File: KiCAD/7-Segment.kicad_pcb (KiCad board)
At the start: 2 copper layers, 94.5 x 100 mm, 26 parts, among them J1 3Pin_Fem, J2 3Pin_Male, J3 3Pin_Fem, J4 3Pin_Male, J5 3Pin_Fem, J6 3Pin_Male, J7 3Pin_Fem, J8 3Pin_Male

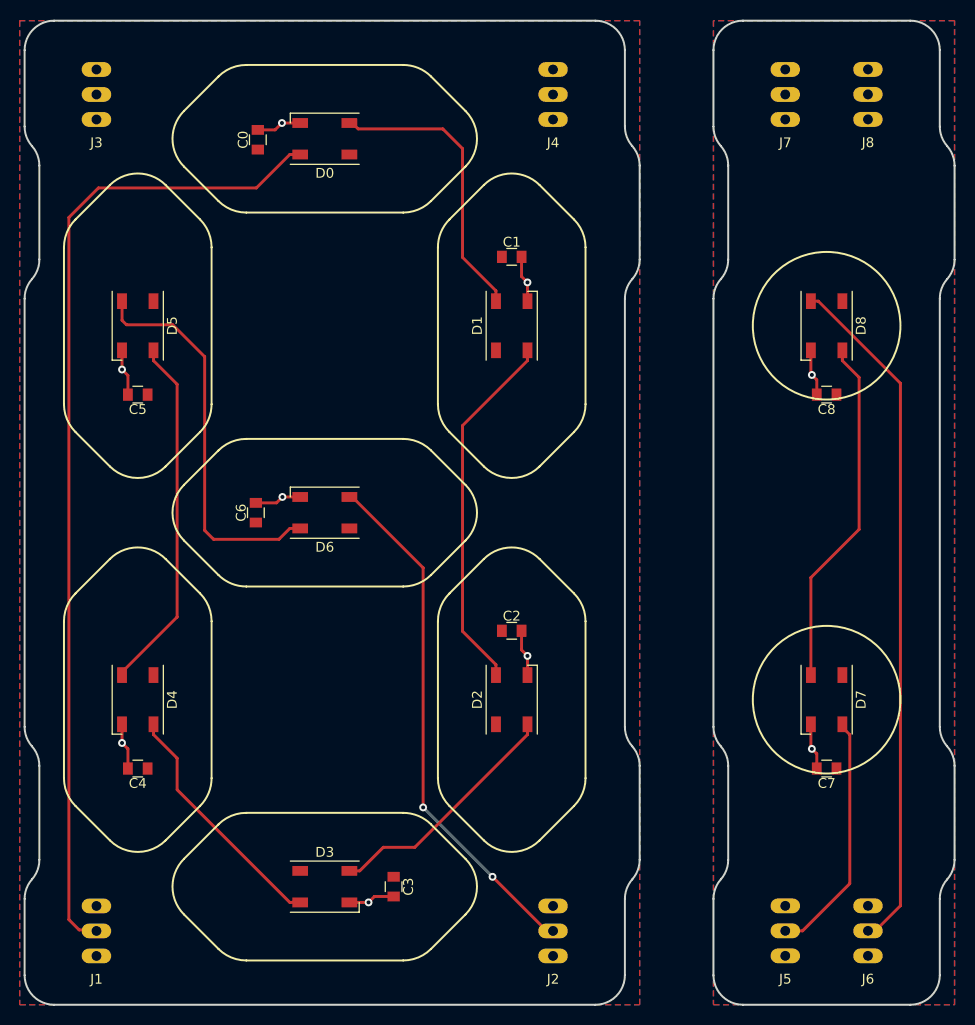
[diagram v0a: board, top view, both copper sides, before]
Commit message: 2-LED per segment
Changed from 1 to 2 LEDs per segment. Removed caps per LED and included 2 placeholder caps for the module.
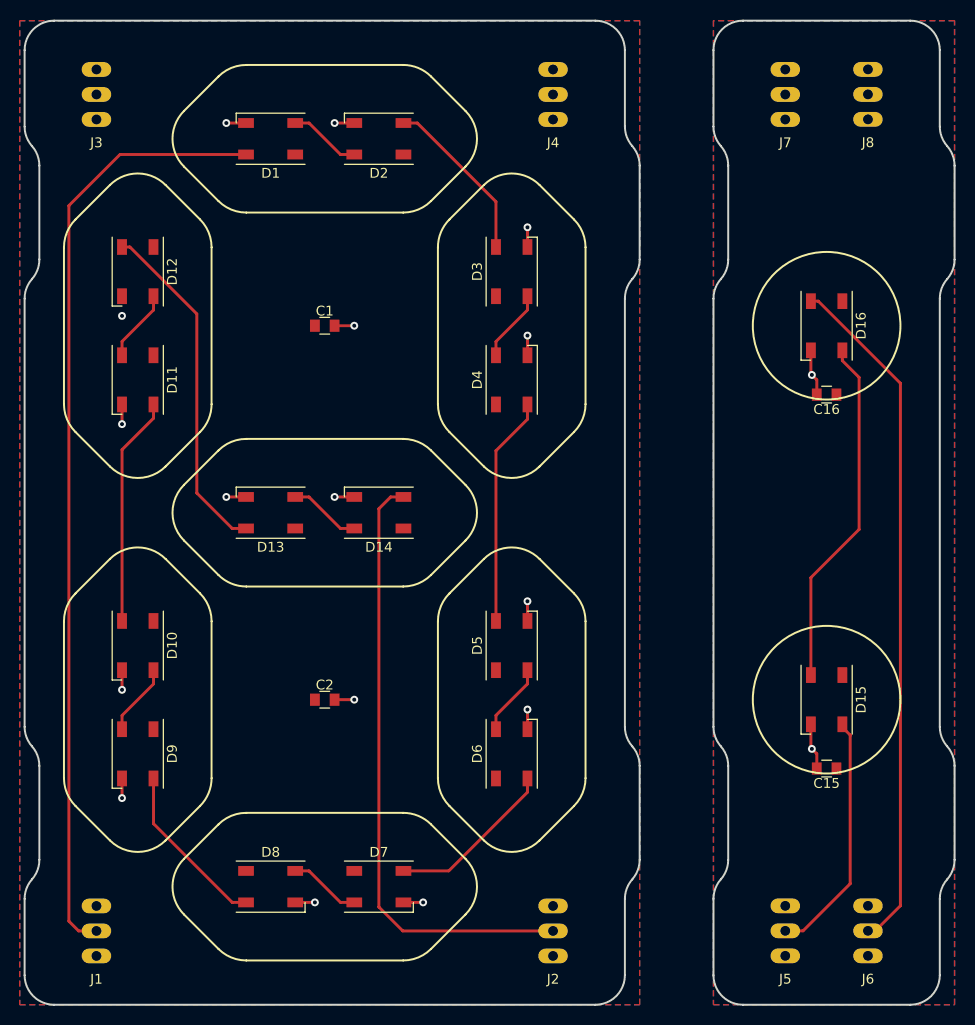
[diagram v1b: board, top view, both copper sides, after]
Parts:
- removed C0, C3, C4, C5, C6, C7, C8: C_Small, Capacitors_SMD:C_0805
- removed D0: WS2812B, LEDs:LED_WS2812B-PLCC4
- added C15: C_Small, Capacitors_SMD:C_0805, F.Cu at (133.0, 125.0)
- added C16: C_Small, Capacitors_SMD:C_0805, F.Cu at (133.0, 87.0)
- added D10: WS2812B, LEDs:LED_WS2812B-PLCC4, F.Cu at (63.0, 112.5)
- added D11: WS2812B, LEDs:LED_WS2812B-PLCC4, F.Cu at (63.0, 85.5)
- added D12: WS2812B, LEDs:LED_WS2812B-PLCC4, F.Cu at (63.0, 74.5)
- added D13: WS2812B, LEDs:LED_WS2812B-PLCC4, F.Cu at (76.5, 99.0)
- added D14: WS2812B, LEDs:LED_WS2812B-PLCC4, F.Cu at (87.5, 99.0)
- added D15: WS2812B, LEDs:LED_WS2812B-PLCC4, F.Cu at (133.0, 118.0)
- added D16: WS2812B, LEDs:LED_WS2812B-PLCC4, F.Cu at (133.0, 80.0)
- added D9: WS2812B, LEDs:LED_WS2812B-PLCC4, F.Cu at (63.0, 123.5)
- moved D8 80.3 mm to (76.5, 137.0), turned to 0 degrees
- moved D3 65.3 mm to (101.0, 74.5), turned to 90 degrees
- moved D2 58.6 mm to (87.5, 61.0), turned to 180 degrees
- moved D4 50.0 mm to (101.0, 85.5), turned to 90 degrees
- moved D5 50.0 mm to (101.0, 112.5), turned to 90 degrees
- moved D7 49.3 mm to (87.5, 137.0), turned to 0 degrees
- moved D1 31.0 mm to (76.5, 61.0), turned to 180 degrees
- moved D6 31.0 mm to (101.0, 123.5), turned to 90 degrees
- moved C1 20.2 mm to (82.0, 80.0)
- moved C2 20.2 mm to (82.0, 118.0)
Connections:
- D1 pad 4: Net-(D0-Pad2) -> Net-(D1-Pad4)
- D7 pad 4: Net-(D7-Pad4) -> Net-(D6-Pad2)
- J1 pad 2: Net-(D0-Pad4) -> Net-(D1-Pad4)
- J2 pad 2: Net-(D6-Pad2) -> Net-(D14-Pad2)
- J3 pad 2: Net-(J3-Pad2) -> (no net)
- J4 pad 2: Net-(J4-Pad2) -> (no net)
- J5 pad 2: Net-(D7-Pad4) -> Net-(D15-Pad4)
- J6 pad 2: Net-(D8-Pad2) -> Net-(D16-Pad2)
- J7 pad 2: Net-(J7-Pad2) -> (no net)
- J8 pad 2: Net-(J8-Pad2) -> (no net)
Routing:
- net Net-(D0-Pad4): track 100.7 -> 0.00 mm
- net Net-(D1-Pad4): track 0.00 -> 96.1 mm
- net Net-(D16-Pad2): track 0.00 -> 70.0 mm
- net Net-(D14-Pad2): track 0.00 -> 62.2 mm
- net Net-(D8-Pad2): track 70.0 -> 17.3 mm
- net Net-(D6-Pad2): track 53.2 -> 17.3 mm, vias 2 -> 0
- net Net-(D15-Pad2): track 0.00 -> 35.7 mm
- net Net-(D12-Pad2): track 0.00 -> 35.1 mm
- net Net-(D5-Pad2): track 40.1 -> 7.33 mm
- net Net-(D1-Pad2): track 37.1 -> 7.33 mm
- net Net-(D0-Pad2): track 29.5 -> 0.00 mm
- net Net-(D7-Pad2): track 35.7 -> 7.33 mm
- net Net-(D15-Pad4): track 0.00 -> 25.1 mm
- net Net-(D7-Pad4): track 25.0 -> 0.00 mm
- net Net-(D10-Pad2): track 0.00 -> 23.3 mm
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
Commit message: Iterative updates
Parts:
- C1: value C_Small -> C_Big; footprint Capacitors_SMD:C_0805 -> Capacitors_SMD:CP_Elec_5x5.3
- C15, C16, C2: footprint Capacitors_SMD:C_0805 -> Capacitors_SMD:C_1206
- J1, J2, J3, J4, J5, J6, J7, J8: footprint 7-Segment Lib:Header3Pin_03 -> 7-Segment Lib:Header3Pin_04
- moved C1 38.0 mm to (82.0, 118.0)
- moved C15 12.2 mm to (133.0, 112.8)
- moved C2 5.30 mm to (82.0, 112.7)
- moved C16 1.75 mm to (133.0, 85.2), turned to 0 degrees
- turned D15 to 180 degrees
- turned D16 to 0 degrees
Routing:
- net Net-(D16-Pad2): track 70.0 -> 64.5 mm
- net Net-(D15-Pad2): track 35.7 -> 39.0 mm
- net GND: track 39.8 -> 40.0 mm, vias 18 -> 17
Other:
- board text added: "7-Seg A v1-0 - PancakeLegend 2020"
- board text added: "7-Seg B v1-0 - PancakeLegend 2020"
- board text added: "JLCJLCJLCJLC"
